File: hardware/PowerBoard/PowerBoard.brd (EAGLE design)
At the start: 90 x 56 mm, 134 parts, among them J1 CON-HRS-DM3AT, J2 CON-ZX62R-B-5P, J3 CON-FTSH-105-01-L-DV-K, J4 CON-S2B-PH-SM4-TB, J5 CON-PJ-102A, J6 CON-71741-0002-TOP, M1 MOUNT-HOLE3.3, M2 MOUNT-HOLE3.3, M3 MOUNT-HOLE3.3, M4 MOUNT-HOLE3.3, M5 FIDUCIAL1X2, M6 FIDUCIAL1X2, M7 FIDUCIAL1X2, M8 FIDUCIAL1X2, Q1 SI2323CDS, Q2 SI2312CDS, Q3 SI2333CDS, Q4 SI2333CDS, SW1 SWITCH-SPST, SW2 SWITCH-MS12ASG30, U1 LTC4361-2DC, U10 MAX9938FEUK, U11 MAX9938FEUK, U12 MAX9938FEUK, U13 STM32F10XCXT6, U14 LTC2942-1, U15 USBLC6-2, U2 LTC4085, U3 XC6220B331MR-G, U4 XC6220B331MR-G, U5 XC9236A15DMR-G, U6 MIC94043, U8 MAX9938FEUK, U9 MAX9938FEUK, X1 ECX-2236, X2 ECX-31B

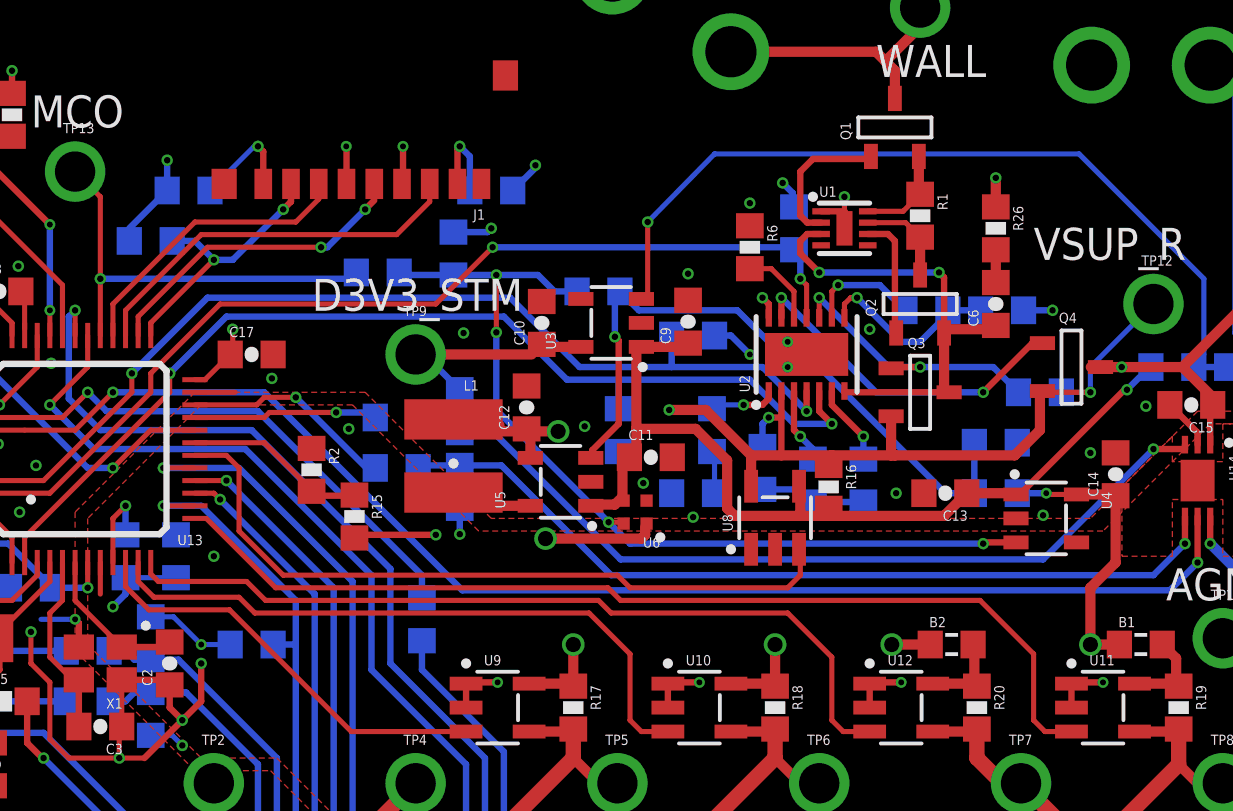
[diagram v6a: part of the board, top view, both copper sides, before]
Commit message: - Filter moved further from ADC lines
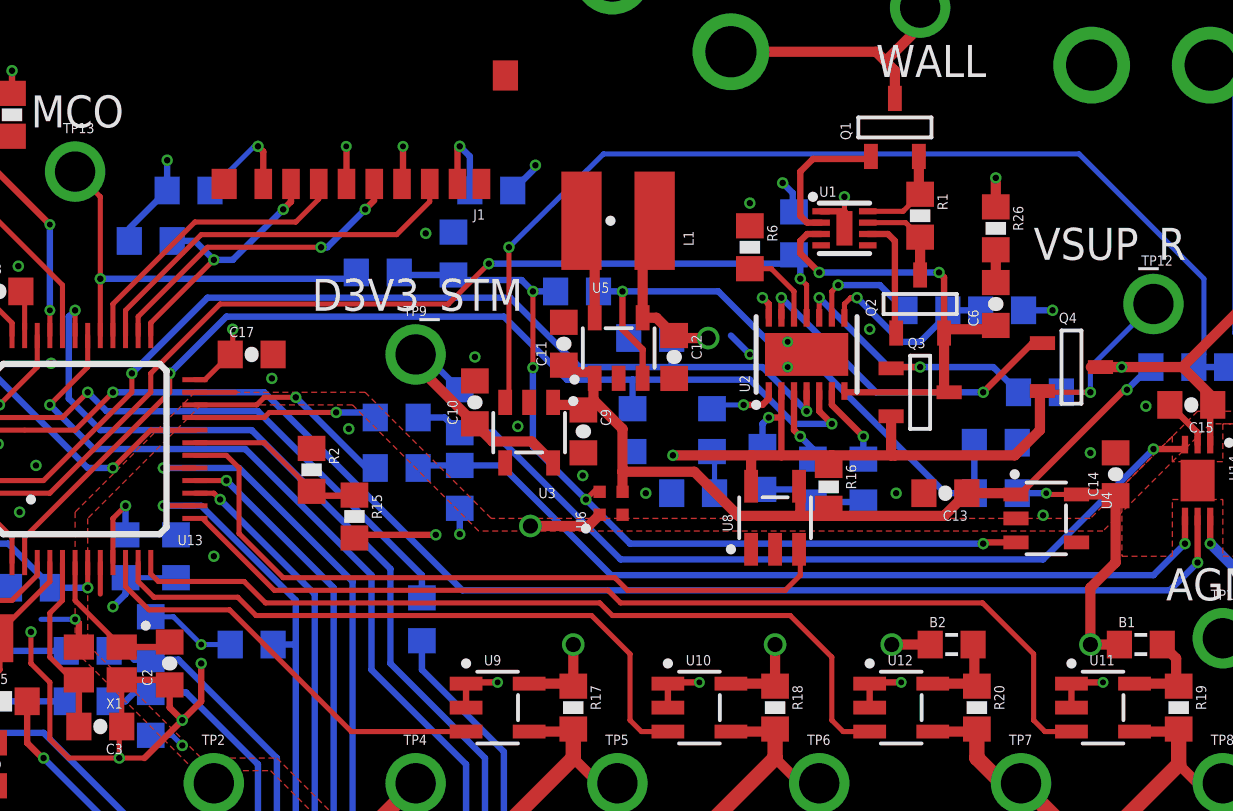
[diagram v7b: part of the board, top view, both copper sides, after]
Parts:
- moved L1 11.4 mm to (45.5, 37.3), turned to 90 degrees
- moved C12 6.18 mm to (47.8, 31.9), turned to 270 degrees
- moved C9 6.01 mm to (44.1, 28.9), turned to 270 degrees
- moved U5 5.78 mm to (45.5, 32.3), turned to 0 degrees
- moved C11 5.67 mm to (43.4, 32.4), turned to 90 degrees
- moved U3 5.43 mm to (42.0, 28.9), turned to 180 degrees
- moved C10 4.12 mm to (39.9, 30.1)
- moved R42 1.70 mm to (46.8, 32.6), turned to 180 degrees
- moved U6 1.01 mm to (45.2, 26.1), turned to 90 degrees
- moved R14 0.85 mm to (43.9, 34.5)
- moved R43 0.55 mm to (46.1, 29.0)
- moved R5 0.20 mm to (52.5, 36.8)
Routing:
- net D3V3_STM-EN: track 32.8 -> 41.4 mm
- net VSUP_I: track 34.0 -> 30.1 mm
- net D1V5-EN: track 26.4 -> 23.5 mm
- net PA8-EN: track 36.6 -> 33.9 mm
- net DGND: track 83.2 -> 81.0 mm, vias 45 -> 44
- net VSUP_R: track 47.7 -> 45.9 mm
- net VSUP: track 36.0 -> 34.9 mm
- net PB9: track 39.9 -> 39.2 mm
- net N$5: track 1.28 -> 1.95 mm
- net D3V3_STM: track 50.5 -> 51.2 mm

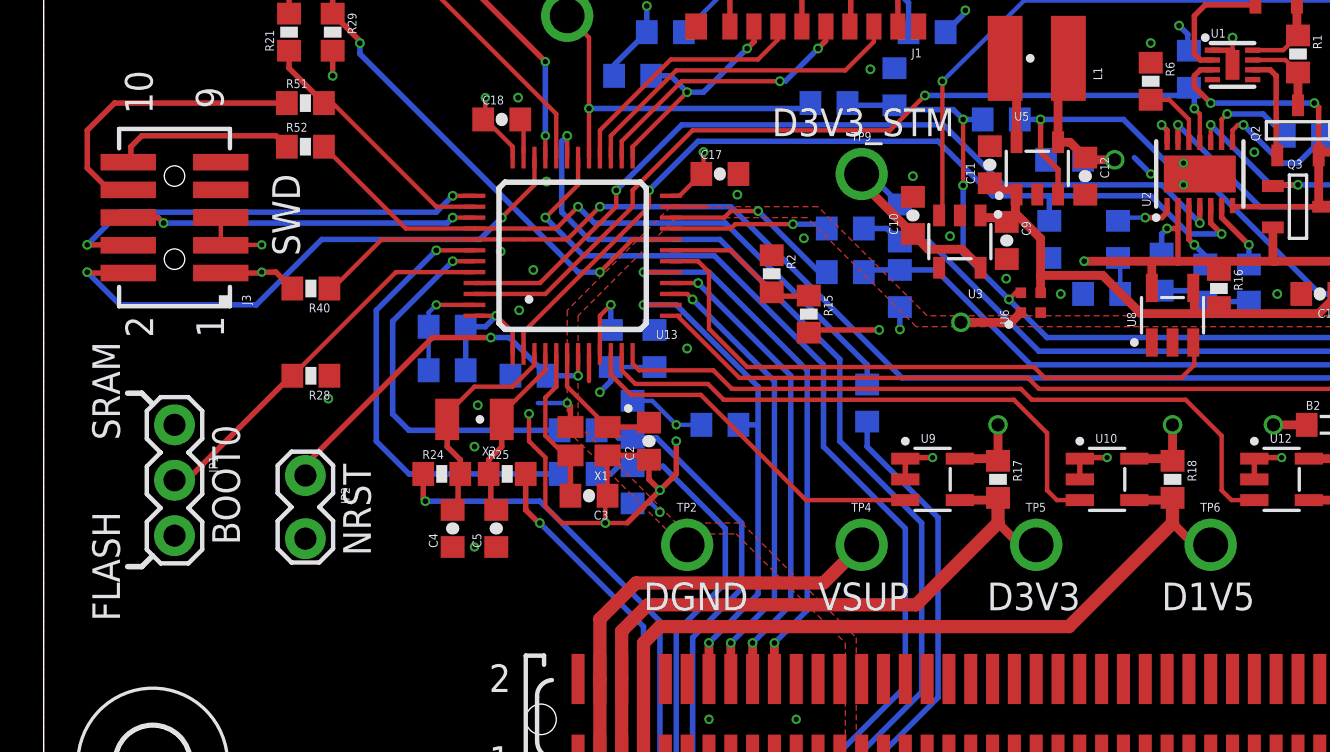
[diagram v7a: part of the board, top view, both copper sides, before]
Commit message: - Pushbutton added for reset
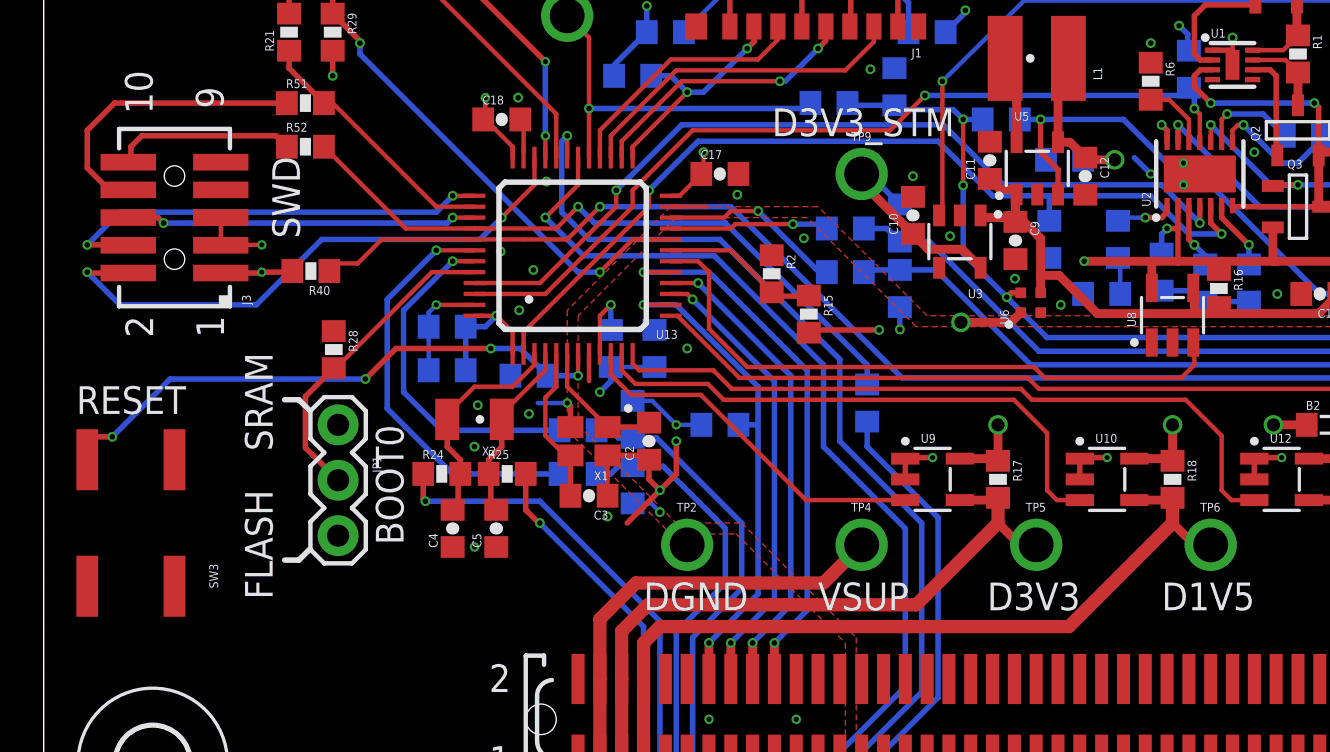
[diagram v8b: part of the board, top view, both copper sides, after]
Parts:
- removed JP2: JUMPER-2PTH-LOCK, powerboard:1X02-LOCK
- added SW3: SWITCH-KSC-201J, powerboard:SWITCH-KSC-J-LEAD
- moved JP1 7.50 mm to (13.5, 20.5)
- moved R28 1.59 mm to (13.3, 23.9), turned to 270 degrees
- moved R40 0.80 mm to (12.2, 27.6)
- moved C9 0.40 mm to (44.5, 28.9)
- moved C11 0.20 mm to (43.4, 32.6)
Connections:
- net DGND: now also SW3.2$1, SW3.2$2; no longer JP2.2
- net NRST: now also SW3.1$1, SW3.1$2; no longer JP2.1
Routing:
- net DGND: track 81.0 -> 71.1 mm, vias 44 -> 43
- net NRST: track 17.1 -> 25.2 mm, vias 2 -> 4
- net BOOT0: track 17.7 -> 14.5 mm
- net I2C1_SCLI: track 20.7 -> 19.1 mm
- net I2C1_SDAI: track 17.1 -> 15.8 mm
- net PB5: track 62.2 -> 61.3 mm
- net VSUP_I: track 30.1 -> 30.6 mm
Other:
- board text added: "RESET"
- board text removed: "NRST"
